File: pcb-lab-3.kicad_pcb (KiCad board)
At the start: 2 copper layers, 93 parts, among them J1 USB_B_Micro, J2 Conn_01x02, J3 Conn_01x02, J301 USB_B_Micro, J302 USB_B_Micro, J303 Conn_01x02, J304 Conn_01x02, J305 Conn_01x02, J306 Conn_01x02, J307 Conn_01x02, J308 Conn_01x02, J309 Conn_01x03_Female, J310 Conn_01x02_Female, J311 Conn_01x03_Female, J4 Conn_01x02, J401 USB_B_Micro, J402 Conn_01x02, J403 Conn_01x02, J404 Conn_01x02, J405 Conn_01x03, J406 Conn_01x03_Female, J407 Conn_01x02, J5 Conn_01x03, J501 Conn_01x02, J502 Conn_01x02, J503 Conn_01x02, J6 Conn_01x04, Q1 Q_NMOS_GSD, Q301 Q_NMOS_GSD, Q302 Q_NMOS_GSD, Q401 Q_NMOS_GSD, U1 NCS2333, U2 MCP4011, U301 NCS2333, U302 INA181, U401 NCS2333, U402 INA181, U501 BCR421U

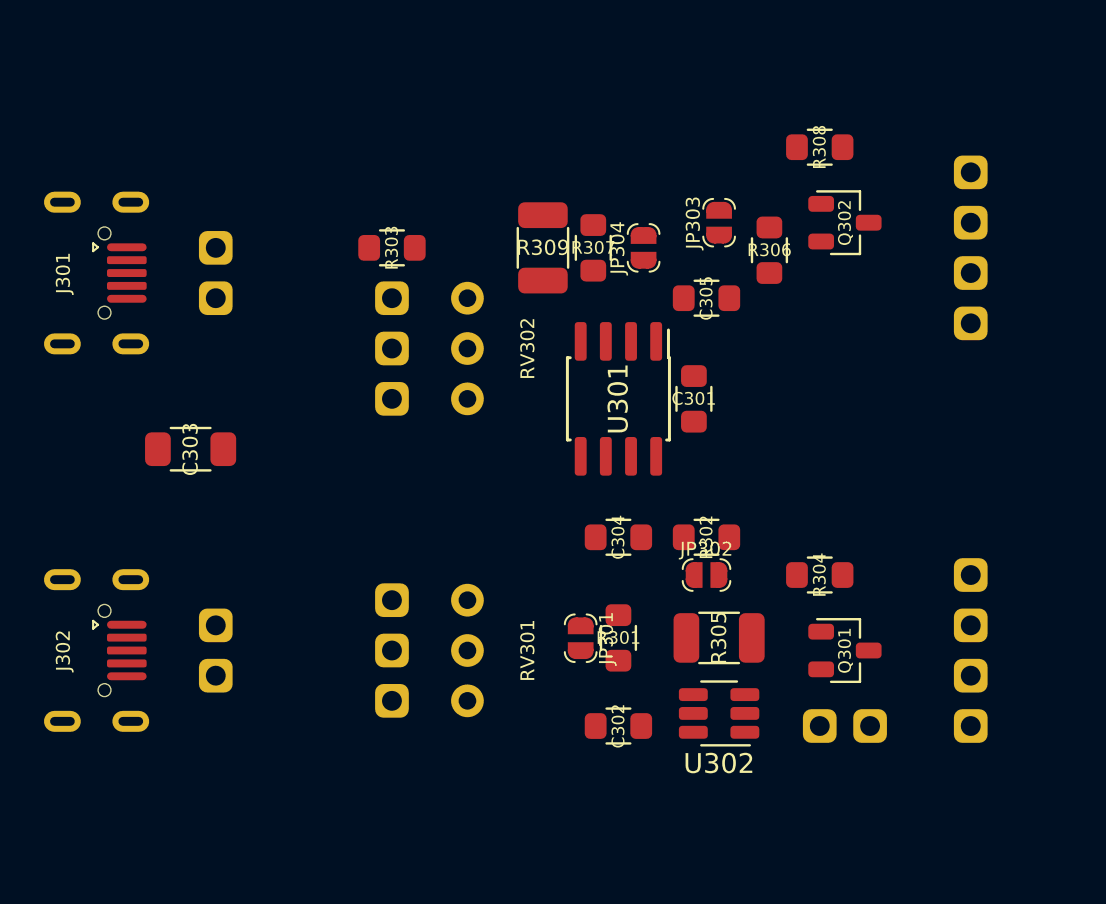
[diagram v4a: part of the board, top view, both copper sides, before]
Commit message: Tuned layout of 2nd circuit
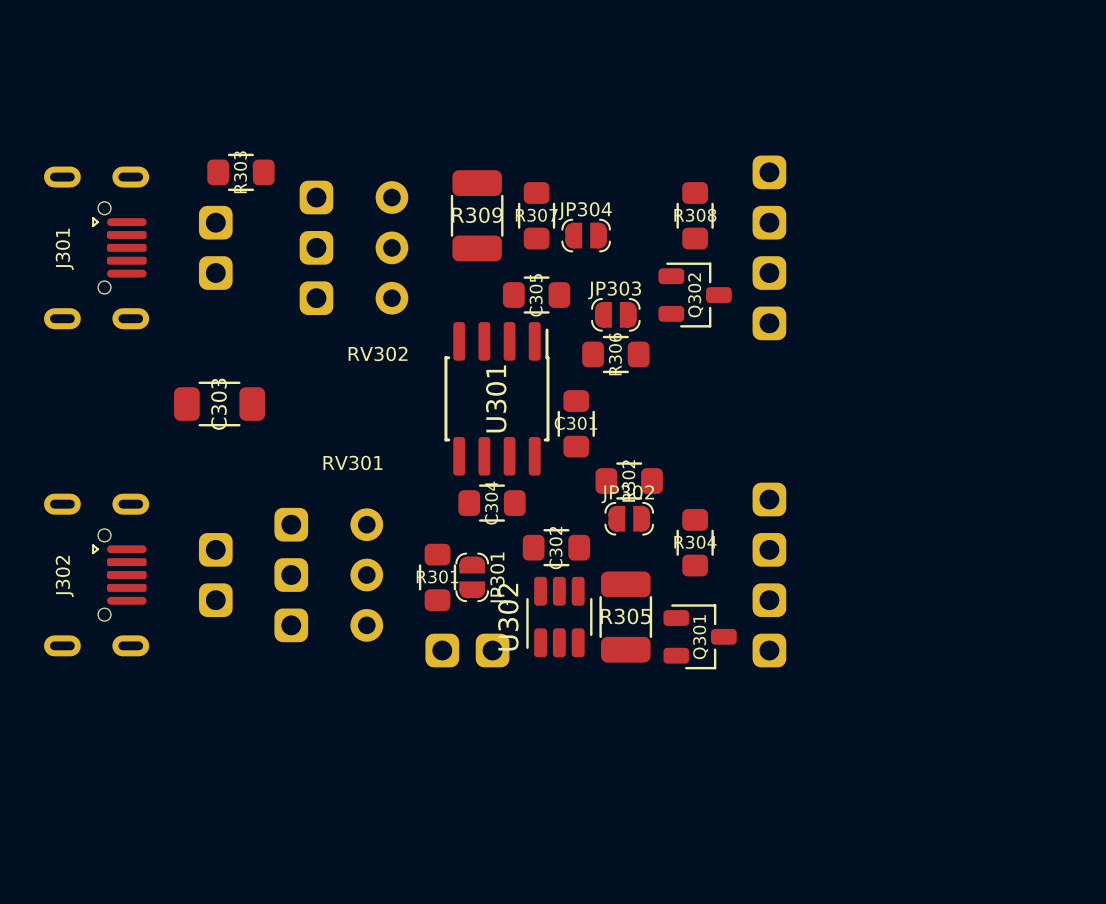
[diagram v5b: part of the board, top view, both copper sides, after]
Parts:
- moved J310 21.9 mm to (142.2, 91.4), turned to 270 degrees
- moved J307 10.9 mm to (158.8, 83.8)
- moved J308 10.9 mm to (158.8, 88.9)
- moved J305 10.2 mm to (158.8, 67.3)
- moved J306 10.2 mm to (158.8, 72.4)
- moved R301 9.63 mm to (142.0, 87.8)
- moved C302 9.53 mm to (148.0, 86.2), turned to 0 degrees
- moved U302 9.41 mm to (148.2, 89.8), turned to 90 degrees
- moved R306 9.37 mm to (151.0, 76.5), turned to 180 degrees
- moved C305 8.58 mm to (147.0, 73.5)
- moved R303 8.52 mm to (132.1, 67.3)
- moved Q302 8.40 mm to (155.0, 73.5)
- moved Q301 7.34 mm to (155.2, 90.8)
- moved R308 7.18 mm to (155.0, 69.5), turned to 270 degrees
- moved JP303 6.98 mm to (151.0, 74.5), turned to 0 degrees
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
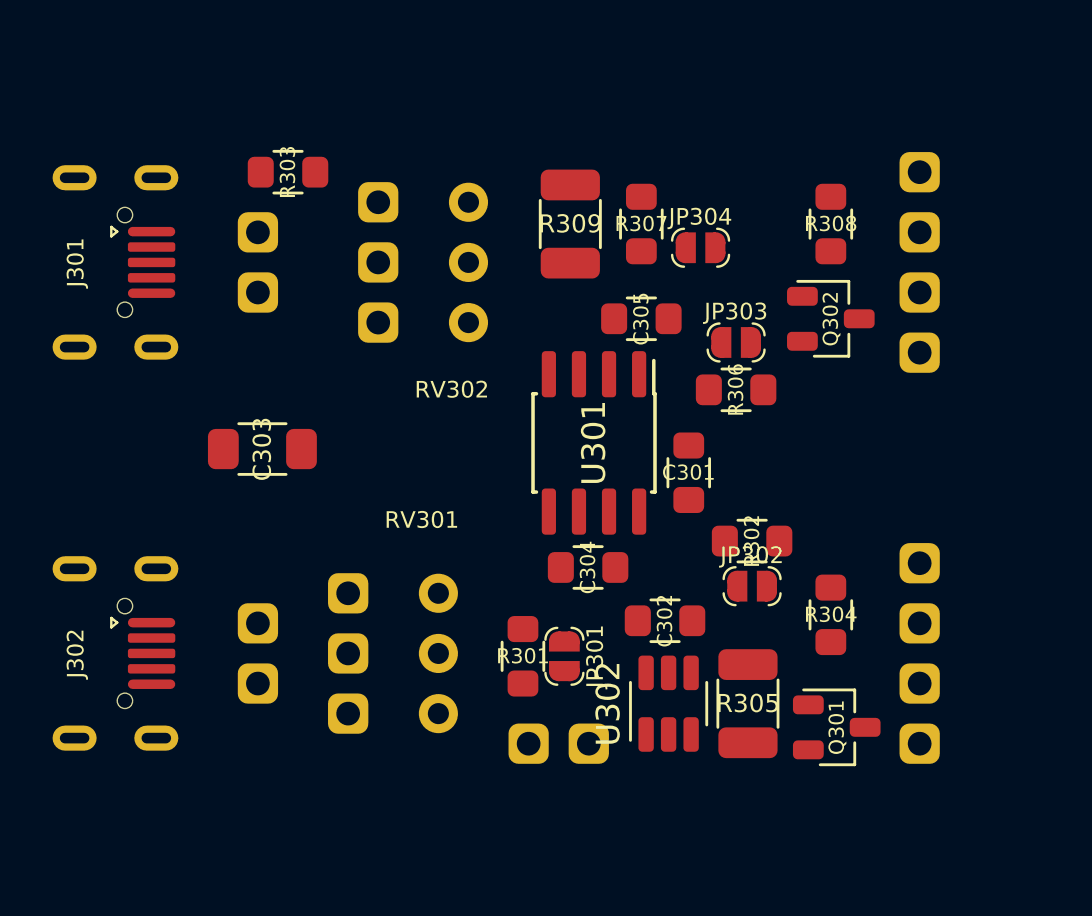
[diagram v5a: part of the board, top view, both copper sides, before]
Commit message: Complete routing (-GND) of 2nd circuit
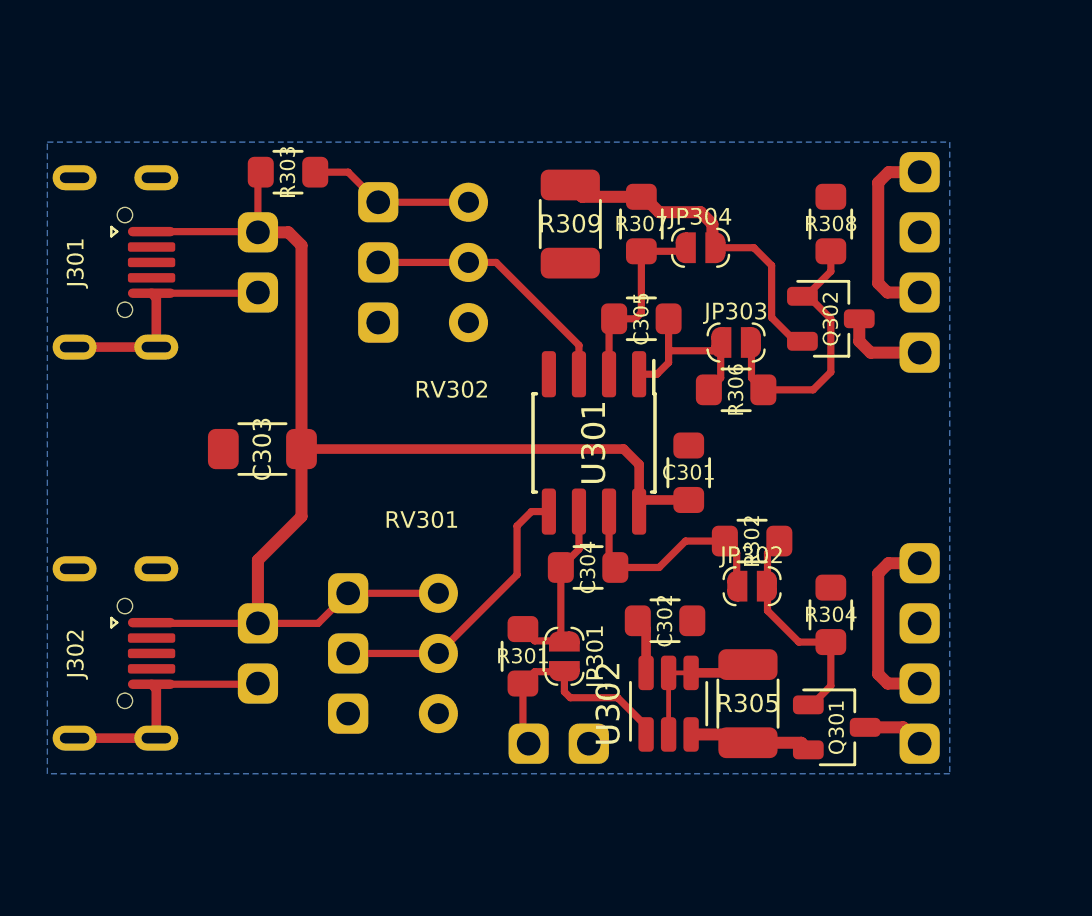
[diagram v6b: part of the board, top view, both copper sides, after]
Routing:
- net +5V: track 57.3 -> 116.7 mm
- net GND: track 15.9 -> 42.6 mm
- net Net-(JP304-Pad2): track 0.00 -> 14.3 mm
- net Net-(J309-Pad2): track 0.00 -> 12.2 mm
- net Net-(J311-Pad2): track 0.00 -> 11.1 mm
- net Net-(JP303-Pad2): track 0.00 -> 10.9 mm
- net Net-(C304-Pad2): track 0.00 -> 9.67 mm
- net Net-(J310-Pad1): track 0.00 -> 9.21 mm
- net Net-(JP302-Pad2): track 0.00 -> 8.93 mm
- net Net-(C305-Pad1): track 0.00 -> 8.19 mm
- net LOAD3+: track 0.00 -> 8.09 mm
- net LOAD2+: track 0.00 -> 8.09 mm
- net Net-(C305-Pad2): track 0.00 -> 7.85 mm
- net Net-(C304-Pad1): track 0.00 -> 7.80 mm
- net Net-(J311-Pad1): track 0.00 -> 7.00 mm
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
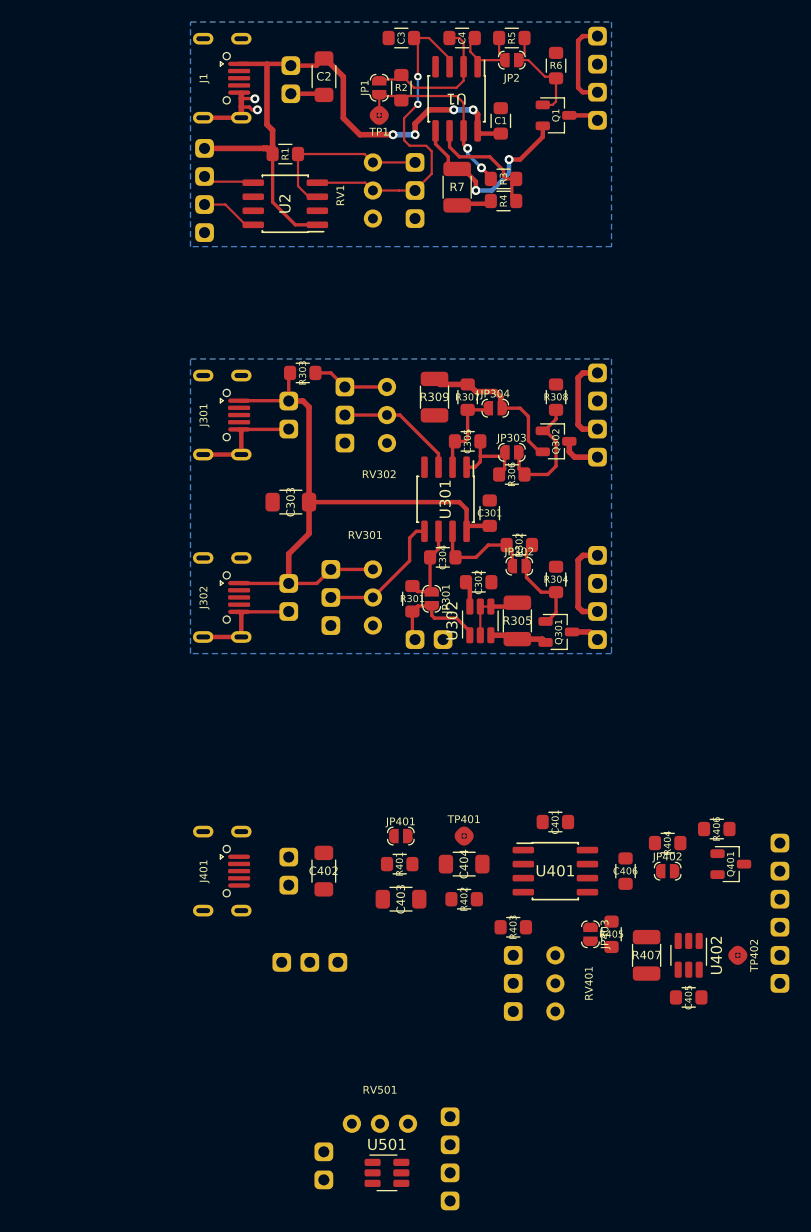
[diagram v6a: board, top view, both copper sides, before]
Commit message: Tune layout of 3rd and 4th circuits
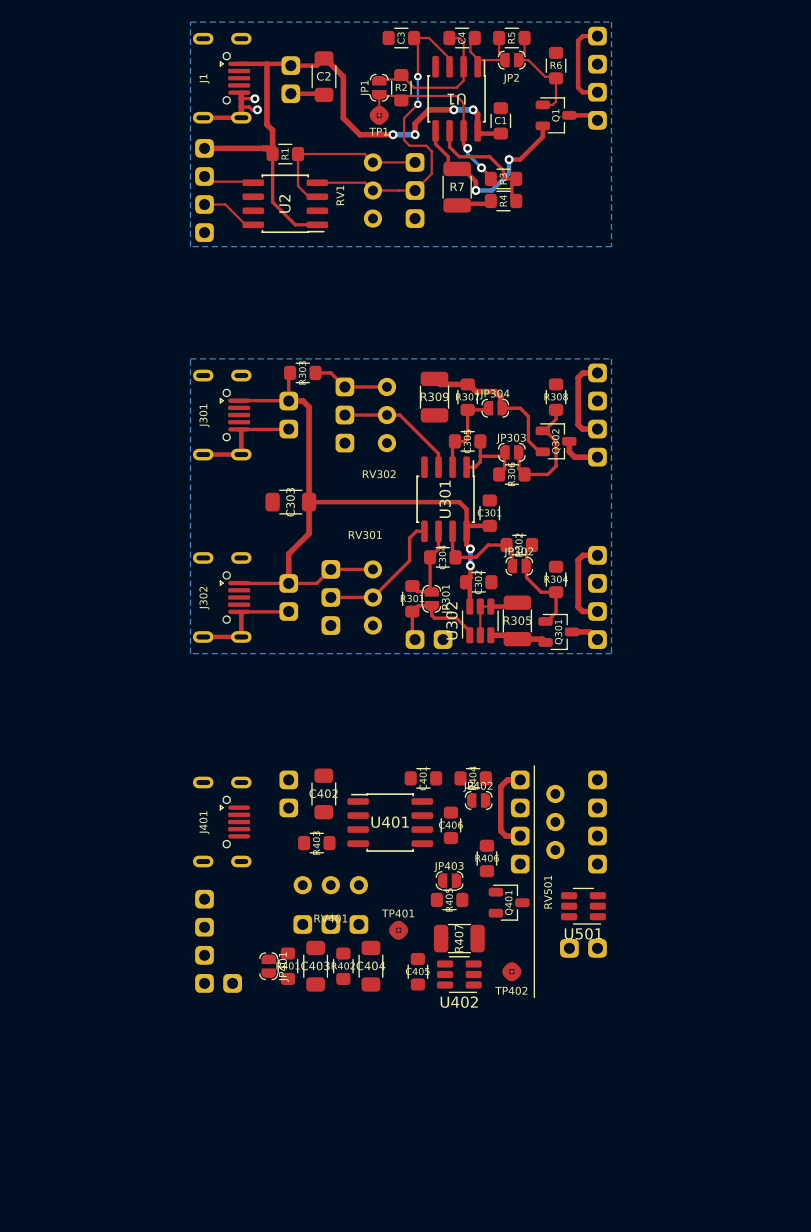
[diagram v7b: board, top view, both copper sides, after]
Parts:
- moved J407 49.6 mm to (125.7, 122.6), turned to 90 degrees
- moved J502 33.3 mm to (158.8, 104.1)
- moved J503 33.3 mm to (158.8, 109.2)
- moved RV501 31.6 mm to (154.9, 108.0), turned to 180 degrees
- moved U501 30.0 mm to (157.5, 115.6), turned to 180 degrees
- moved J501 28.9 mm to (156.2, 119.4), turned to 270 degrees
- moved C405 24.6 mm to (142.5, 121.5), turned to 90 degrees
- moved J403 24.2 mm to (151.8, 104.1)
- moved J404 24.2 mm to (151.8, 109.2)
- moved RV401 22.2 mm to (134.6, 113.7), turned to 270 degrees
- moved R406 21.0 mm to (148.8, 111.2), turned to 270 degrees
- moved U402 20.8 mm to (146.2, 121.8), turned to 180 degrees
- moved TP402 20.5 mm to (151.0, 121.5)
- moved Q401 20.4 mm to (150.8, 115.2)
- moved R403 19.3 mm to (133.3, 109.9), turned to 180 degrees
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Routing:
- net LOAD4+: track 0.00 -> 7.98 mm
- net +5V: track 116.7 -> 121.6 mm, vias 4 -> 6

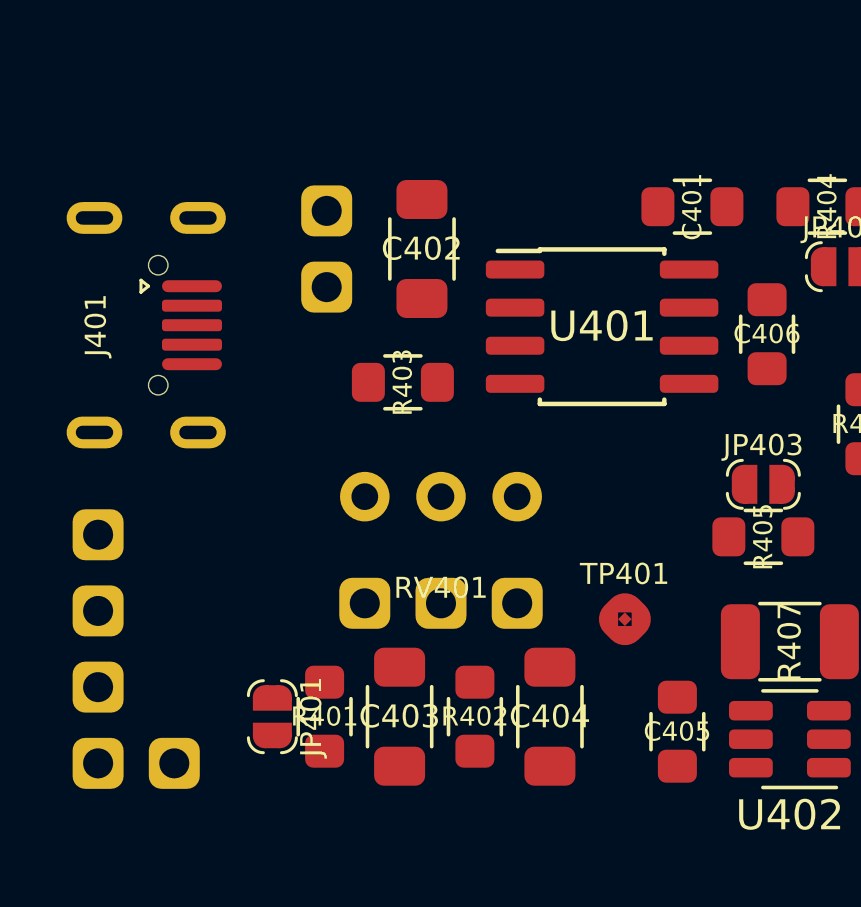
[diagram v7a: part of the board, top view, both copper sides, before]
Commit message: Remove potentiometer from PWM circuit
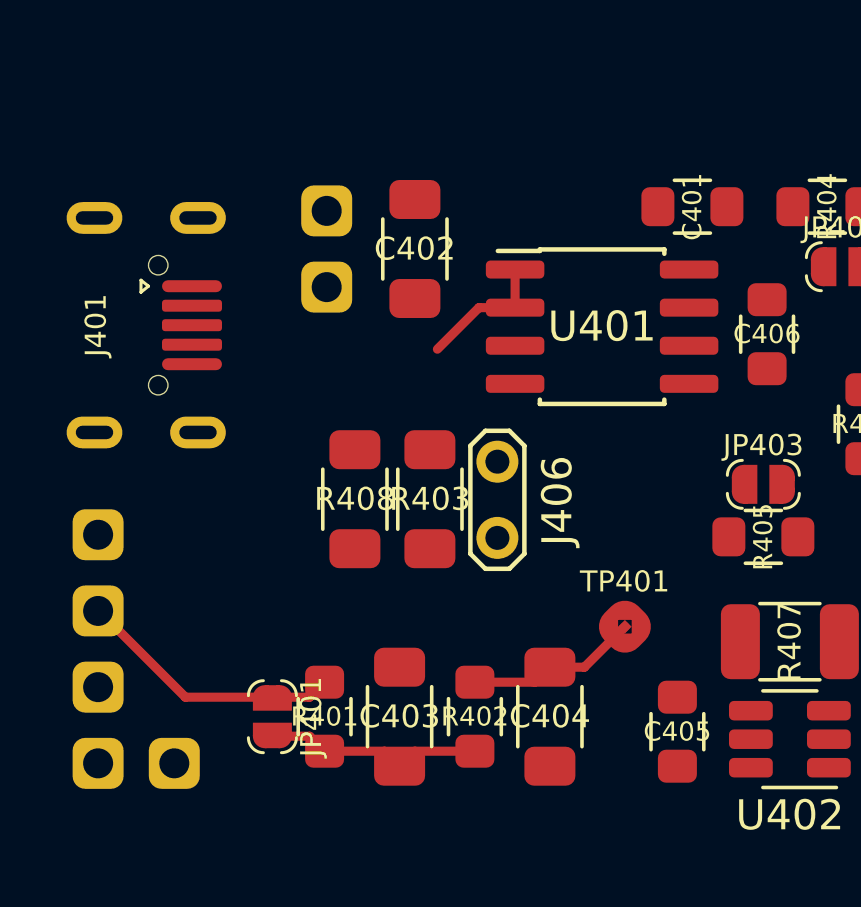
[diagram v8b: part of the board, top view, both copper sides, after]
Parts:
- removed RV401: 1k, local_footprints:RV-Pot_3-pin_2.54mm
- added R408: 100, local_footprints:1206_HS, F.Cu at (131.8, 113.8)
- J406: value Conn_01x03_Female -> Conn_01x02_Female; footprint local_footprints:Pin_Header_Straight_1x03_Pitch2.54mm -> TestPoint:TestPoint_2Pads_Pitch2.54mm_Drill0.8mm
- R403: value 100k -> 10k; footprint local_footprints:0805_HS -> local_footprints:1206_HS
- moved J406 4.77 mm to (136.5, 112.5), turned to 270 degrees
- moved R403 4.00 mm to (134.2, 113.8), turned to 270 degrees
- moved TP401 0.25 mm to (140.8, 118.0)
- moved C402 0.24 mm to (133.8, 105.4)
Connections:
- R403 pad 1: Net-(R403-Pad1) -> Net-(J406-Pad1)
- R403 pad 2: Net-(J406-Pad1) -> Net-(J406-Pad2)
- U401 pad 1: Net-(R403-Pad1) -> Net-(J406-Pad1)
- U401 pad 2: Net-(R403-Pad1) -> Net-(J406-Pad1)
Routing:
- net uC_PWM: track 0.00 -> 8.95 mm
- net Net-(C403-Pad2): track 0.00 -> 7.37 mm
- net Net-(C404-Pad1): track 0.00 -> 5.77 mm
- net Net-(J406-Pad1): track 0.00 -> 4.43 mm
